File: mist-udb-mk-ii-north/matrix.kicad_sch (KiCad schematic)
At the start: 213 parts

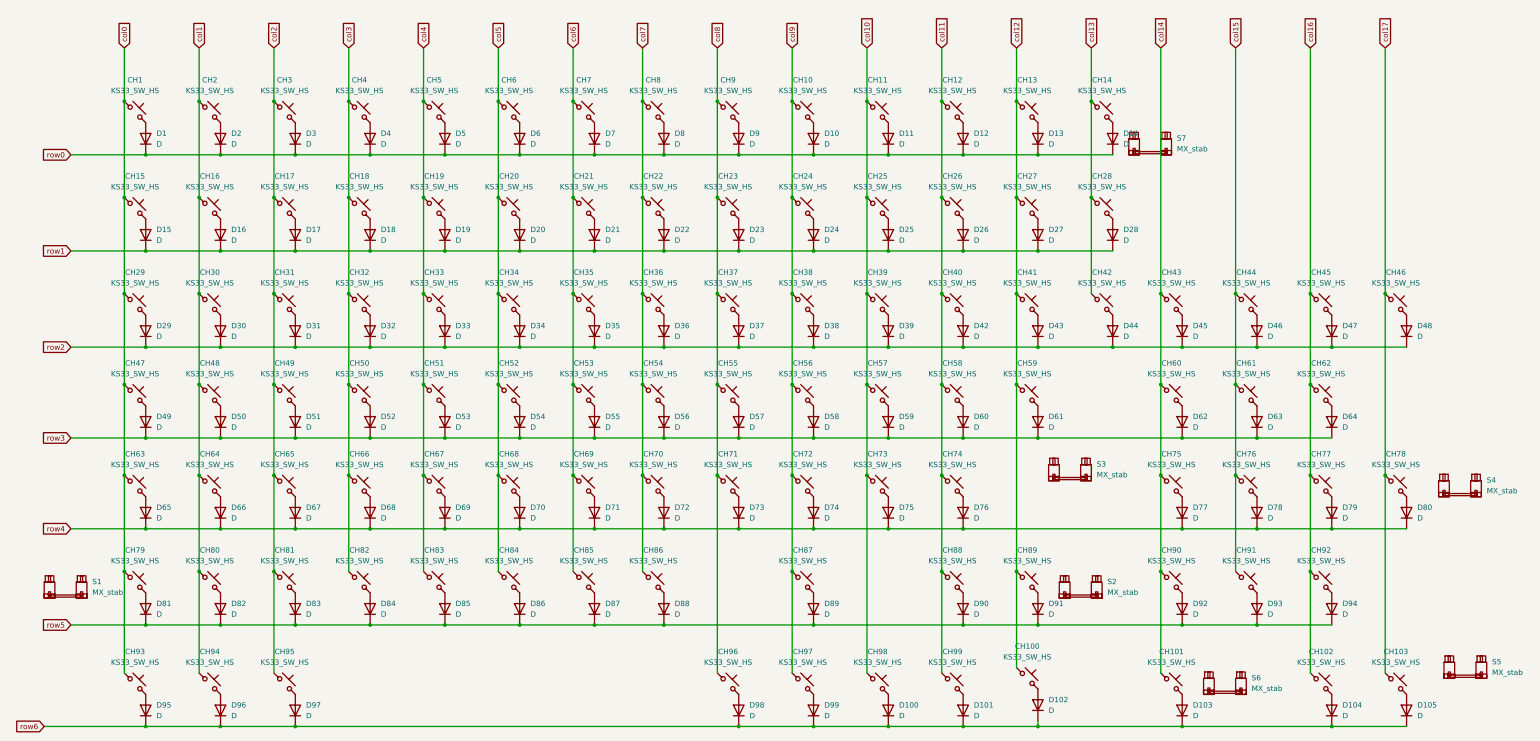
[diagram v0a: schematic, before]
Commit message: Fixed cap annotations
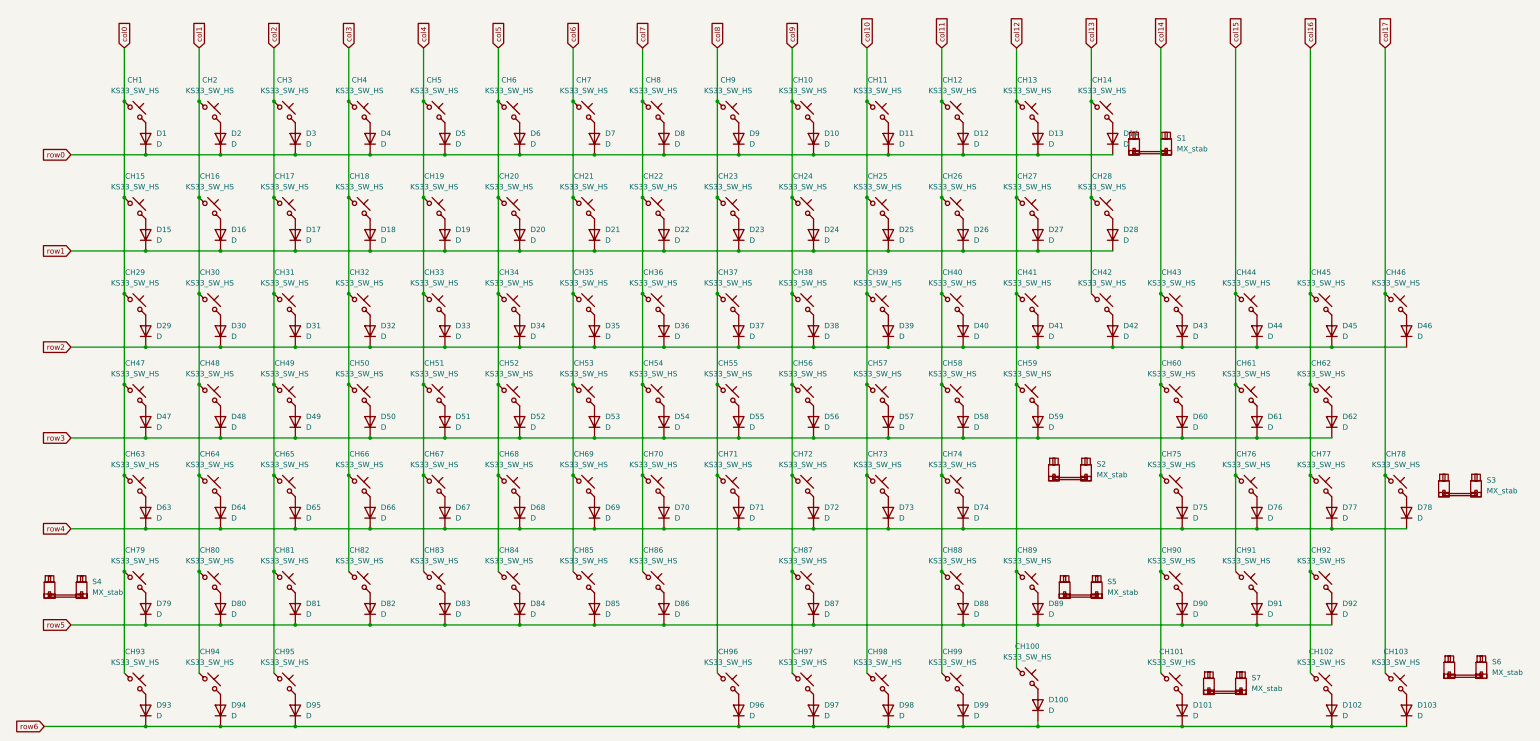
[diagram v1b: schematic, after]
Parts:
- renumbered D102 to D100, D103 to D101, D104 to D102, D105 to D103, D42 to D40, D43 to D41, D44 to D42, D45 to D43, D46 to D44, D47 to D45, D48 to D46, D49 to D47, D50 to D48, D51 to D49, D52 to D50, D53 to D51, D54 to D52, D55 to D53, D56 to D54, D57 to D55, D58 to D56, D59 to D57, D60 to D58, D61 to D59, D62 to D60, D63 to D61, D64 to D62, D65 to D63, D66 to D64, D67 to D65, D68 to D66, D69 to D67, D70 to D68, D71 to D69, D72 to D70, D73 to D71, D74 to D72, D75 to D73, D76 to D74, D77 to D75, D78 to D76, D79 to D77, D80 to D78, D81 to D79, D82 to D80, D83 to D81, D84 to D82, D85 to D83, D86 to D84, D87 to D85, D88 to D86, D89 to D87, D90 to D88, D91 to D89, D92 to D90, D93 to D91, D94 to D92, D95 to D93, D96 to D94, D97 to D95, D98 to D96, D99 to D97, D100 to D98, D101 to D99, S7 to S1, S3 to S2, S4 to S3, S1 to S4, S2 to S5, S5 to S6, S6 to S7

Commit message: Cleaned up mist, added better stab footprints
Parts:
- S1, S3, S6, S7: footprint PCM_marbastlib-mx:STAB_MX_P_2u -> ModHob:KS33_MX_STAB_COMBO
- S2, S4: footprint PCM_marbastlib-mx:STAB_MX_P_2.25u -> ModHob:KS33_MX_STAB_COMBO
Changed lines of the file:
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@@
 			)
 		)
-		(property "Footprint" "PCM_marbastlib-mx:STAB_MX_P_2u"
+		(property "Footprint" "ModHob:KS33_MX_STAB_COMBO"
 			(at 388.62 154.94 0)
 			(effects
@@
 			)
 		)
-		(property "Footprint" "PCM_marbastlib-mx:STAB_MX_P_2u"
+		(property "Footprint" "ModHob:KS33_MX_STAB_COMBO"
 			(at 389.89 198.12 0)
 			(effects
@@
 			)
 		)
-		(property "Footprint" "PCM_marbastlib-mx:STAB_MX_P_2.25u"
+		(property "Footprint" "ModHob:KS33_MX_STAB_COMBO"
 			(at 295.91 151.13 0)
 			(effects
@@
 			)
 		)
-		(property "Footprint" "PCM_marbastlib-mx:STAB_MX_P_2u"
+		(property "Footprint" "ModHob:KS33_MX_STAB_COMBO"
 			(at 332.74 201.93 0)
 			(effects
@@
 			)
 		)
-		(property "Footprint" "PCM_marbastlib-mx:STAB_MX_P_2.25u"
+		(property "Footprint" "ModHob:KS33_MX_STAB_COMBO"
 			(at 57.15 179.07 0)
 			(effects
@@
 			)
 		)
-		(property "Footprint" "PCM_marbastlib-mx:STAB_MX_P_2u"
+		(property "Footprint" "ModHob:KS33_MX_STAB_COMBO"
 			(at 314.96 73.66 0)
 			(effects
